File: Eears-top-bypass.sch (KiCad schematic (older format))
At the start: 124 parts

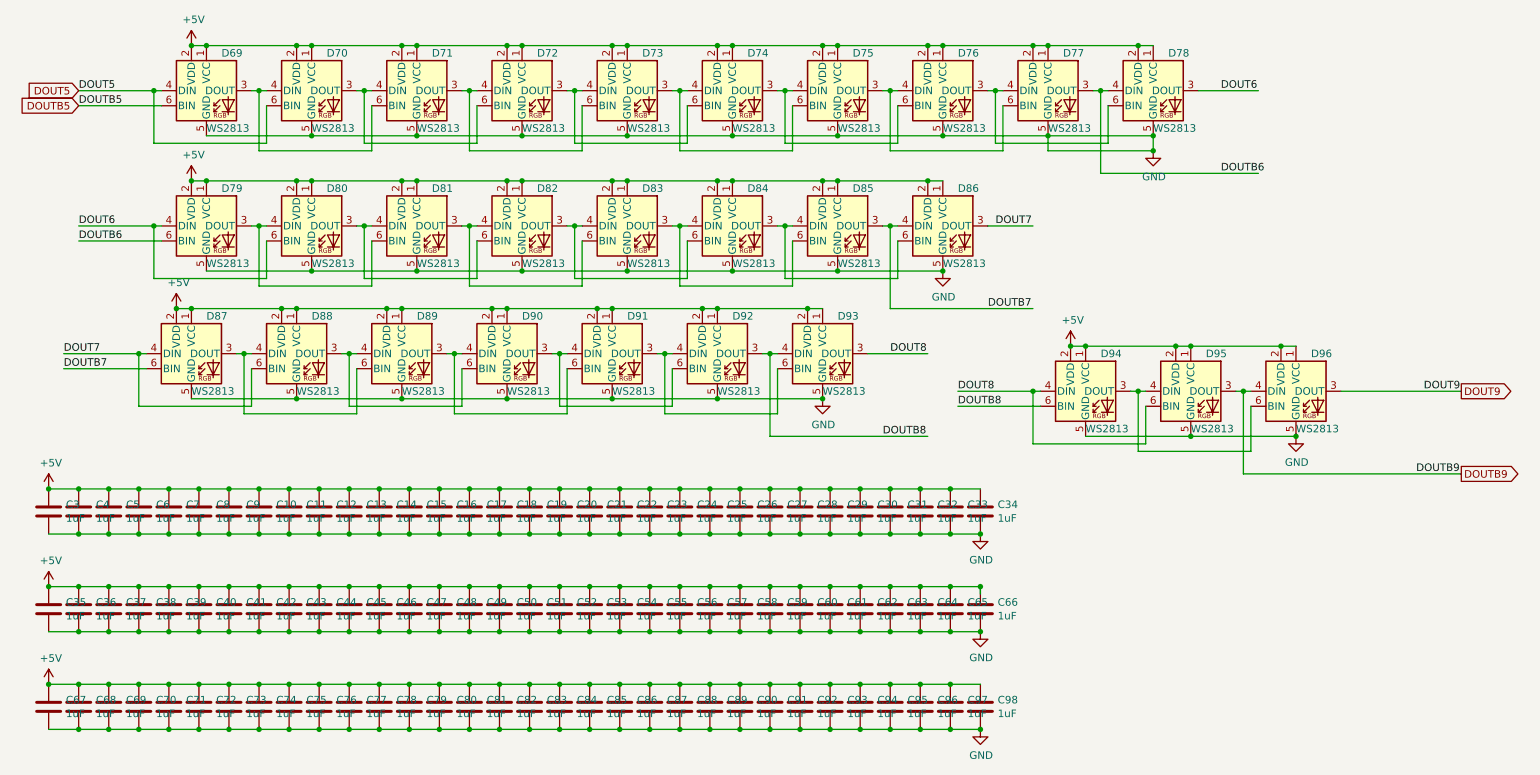
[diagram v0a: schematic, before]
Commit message: Cleaned up ears and added protection diode.
The diode should short things out should power and ground be
reversed.

Added new footprint for WS2813B-Minis.  Note that this footprint has
not yet been tested.

Signed-off-by: aaronw <aaron.w2@gmail.com>
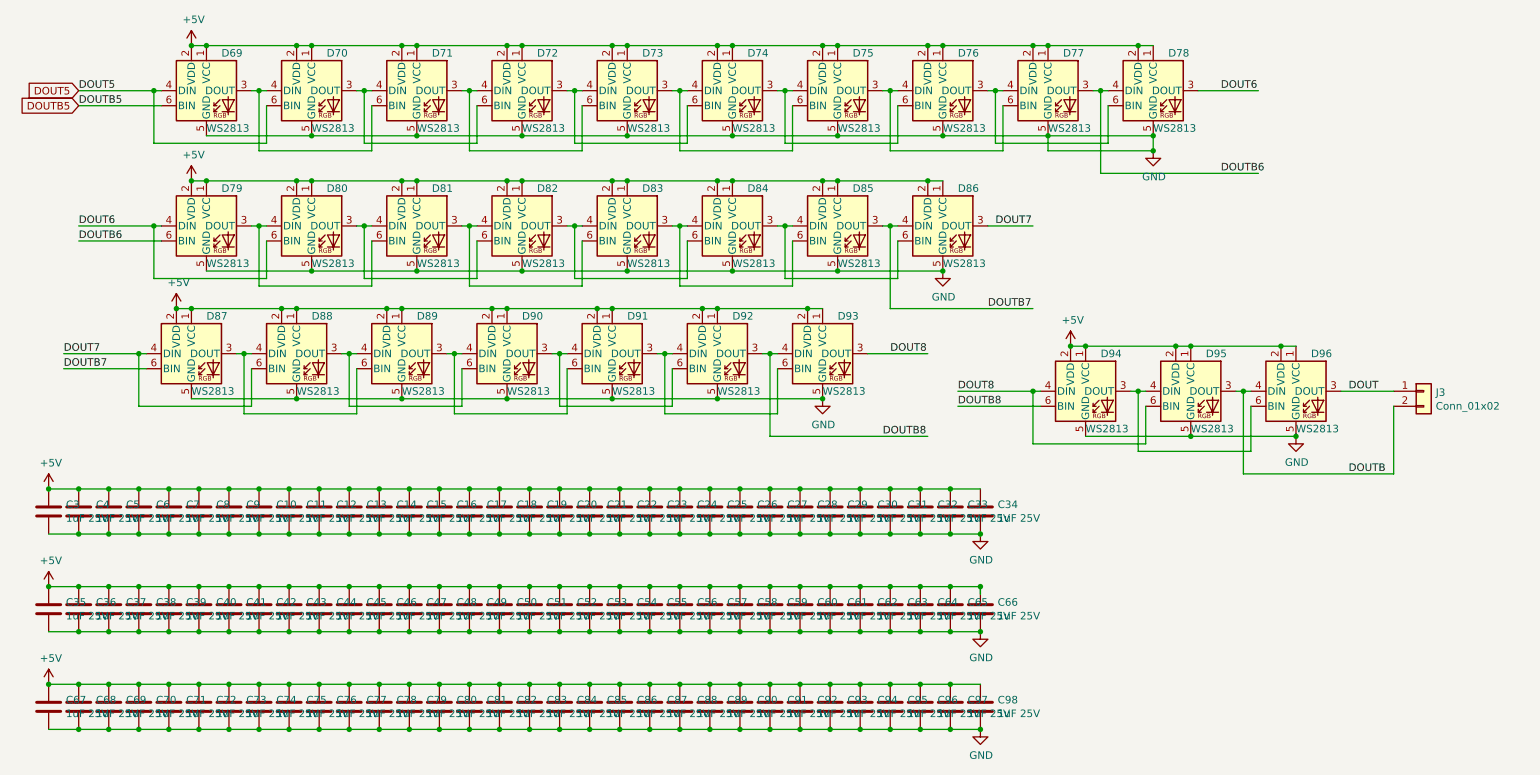
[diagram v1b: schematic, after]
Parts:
- added J3: Conn_01x02, Connector_PinHeader_2.54mm:PinHeader_1x02_P2.54mm_Vertical, symbol Connector_Generic:Conn_01x02
- C10, C11, C12, C13, C14, C15, C16, C17, C18, C19, C20, C21, C22, C23, C24, C25, C26, C27, C28, C29, C3, C30, C31, C32, C33, C34, C35, C36, C37, C38, C39, C4, C40, C41, C42, C43, C44, C45, C46, C47, C48, C49, C5, C50, C51, C52, C53, C54, C55, C56, C57, C58, C59, C6, C60, C61, C62, C63, C64, C65, C66, C67, C68, C69, C7, C70, C71, C72, C73, C74, C75, C76, C77, C78, C79, C8, C80, C81, C82, C83, C84, C85, C86, C87, C88, C89, C9, C90, C91, C92, C93, C94, C95, C96, C97, C98: value 1uF -> 1uF 25V; MFR (none) -> Samsung; MPN (none) -> CL10B105KA8NNNC; SPN (none) -> 1276-1184-1-ND; SPR (none) -> Digikey; SPURL (none) -> -
- D69, D70, D71, D72, D73, D74, D75, D76, D77, D78, D79, D80, D81, D82, D83, D84, D85, D86, D87, D88, D89, D90, D91, D92, D93, D94, D95, D96: MFR (none) -> World Semi; MPN (none) -> WS2813B-Mini; SPN (none) -> -; SPR (none) -> -; SPURL (none) -> -
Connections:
- net DOUT9 renamed DOUT
- net DOUT: now also J3.1 (Pin_1)
- net DOUTB9 renamed DOUTB
- net DOUTB: now also J3.2 (Pin_2)
